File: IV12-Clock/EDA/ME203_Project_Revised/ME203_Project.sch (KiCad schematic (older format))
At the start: 27 parts, among them J1 Conn_01x12, J10 Conn_01x01, J11 Conn_01x02, J12 Conn_01x01, J13 Conn_01x02, J2 Conn_01x05, J6 Conn_01x07

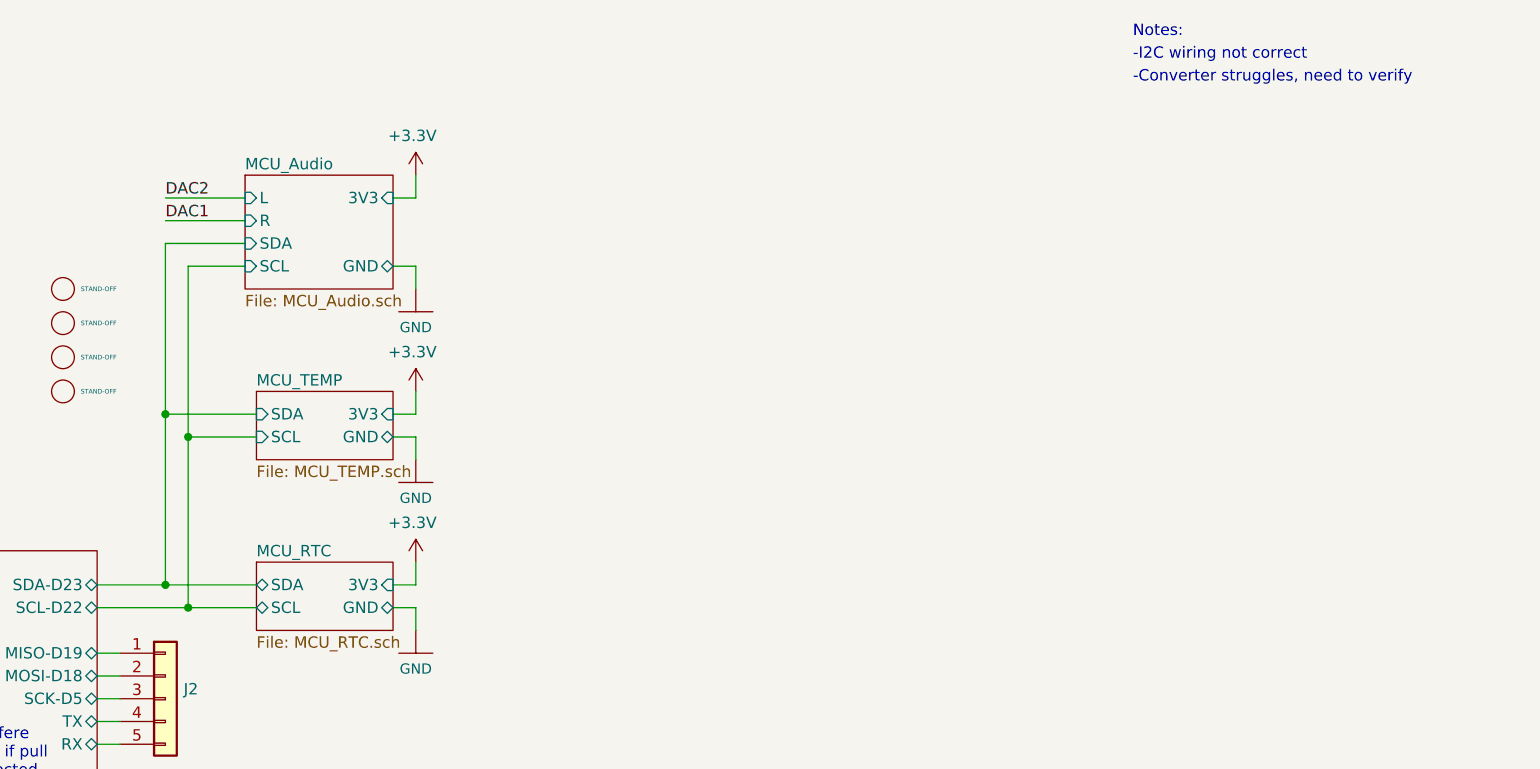
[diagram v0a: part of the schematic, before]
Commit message: Added touch buttons for speakers (untested)
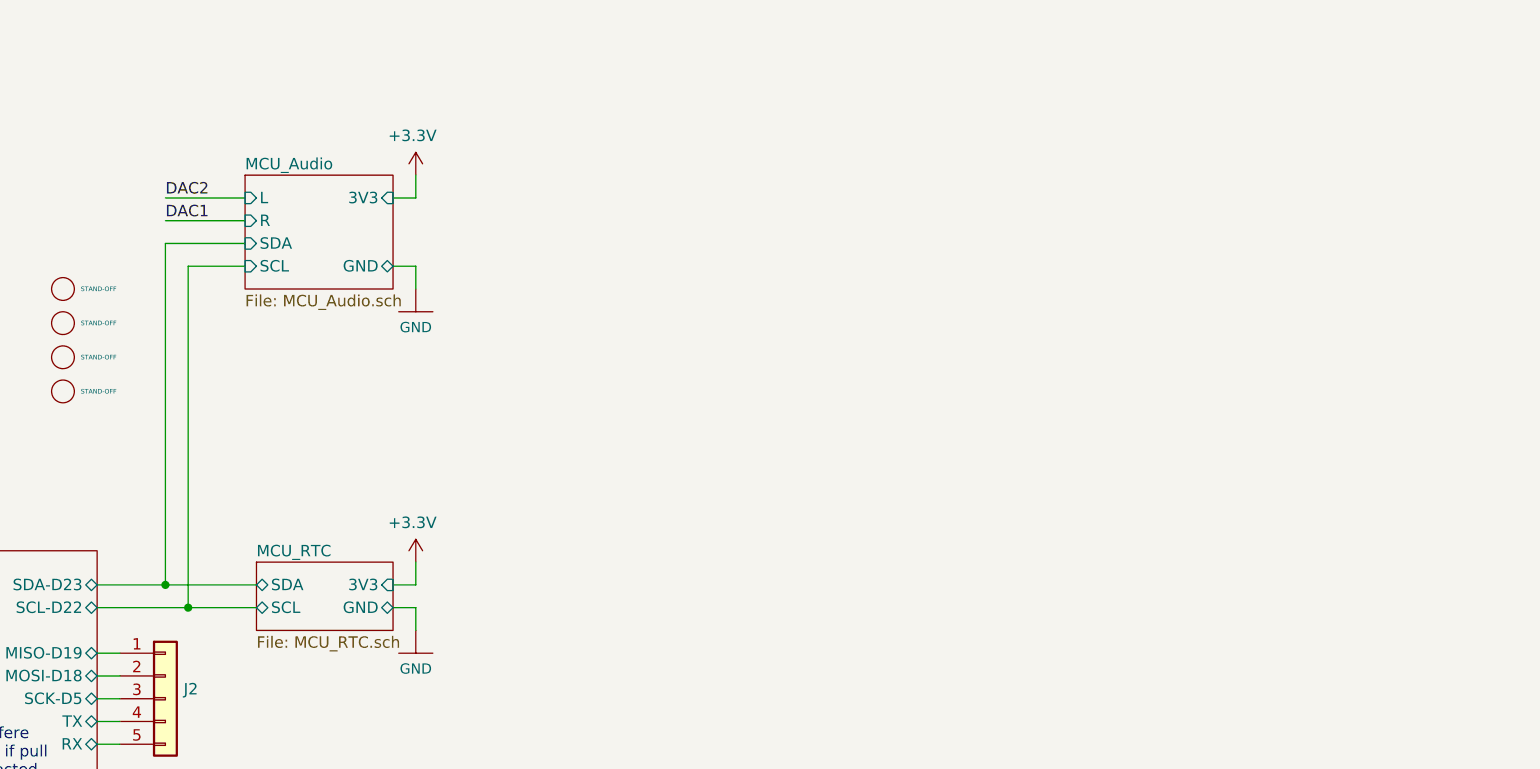
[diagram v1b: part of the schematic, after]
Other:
- note removed: "-Converter struggles, need to verify"
- note removed: "-I2C wiring not correct"
- note removed: "Notes:"
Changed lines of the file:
@@
 $Descr A4 11693 8268
 encoding utf-8
-Sheet 1 8
+Sheet 1 7
 Title ""
 Date ""
@@
 Wire Wire Line
 	2800 4500 2800 4600
-$Sheet
-S 5900 2250 600  300
-U 5CCEB9C5
-F0 "MCU_TEMP" 50
-F1 "MCU_TEMP.sch" 50
-F2 "SCL" I L 5900 2450 50
-F3 "GND" B R 6500 2450 50
-F4 "3V3" I R 6500 2350 50
-F5 "SDA" I L 5900 2350 50
-$EndSheet
 $Comp
 L SparkFun-PowerSymbols:GND #GND0123
@@
 	1    0    0    -1
 $EndComp
-Wire Wire Line
-	6600 2250 6600 2350
-Wire Wire Line
-	6600 2450 6600 2550
-$Comp
-L power:+3.3V #PWR0122
-U 1 1 5CCF9E67
-P 6600 2250
-F 0 "#PWR0122" H 6600 2100 50  0001 C CNN
-F 1 "+3.3V" H 6615 2423 50  0000 C CNN
-F 2 "" H 6600 2250 50  0001 C CNN
-F 3 "" H 6600 2250 50  0001 C CNN
-	1    6600 2250
-	-1   0    0    -1
-$EndComp
-$Comp
-L SparkFun-PowerSymbols:GND #GND0124
-U 1 1 5CCF9E6D
-P 6600 2550
-F 0 "#GND0124" H 6650 2500 45  0001 L BNN
-F 1 "GND" H 6600 2381 45  0000 C CNN
-F 2 "" H 6600 2450 60  0001 C CNN
-F 3 "" H 6600 2450 60  0001 C CNN
-	1    6600 2550
-	1    0    0    -1
-$EndComp
-Wire Wire Line
-	6500 2450 6600 2450
-Wire Wire Line
-	6600 2350 6500 2350
-Wire Wire Line
-	5500 3100 5500 2350
-Wire Wire Line
-	5500 2350 5900 2350
 Connection ~ 5500 3100
 Wire Wire Line
 	5500 3100 5900 3100
-Wire Wire Line
-	5900 2450 5600 2450
-Wire Wire Line
-	5600 2450 5600 3200
 Connection ~ 5600 3200
 Wire Wire Line
@@
 F7 "3V3" I R 6500 1400 50
 $EndSheet
-Connection ~ 5600 2450
-Connection ~ 5500 2350
-Wire Wire Line
-	5600 1700 5600 2450
-Wire Wire Line
-	5500 1600 5500 2350
 Wire Wire Line
 	5600 1700 5850 1700
@@
 	1    0    0    -1
 $EndComp
-Text Notes 9750 700  0    50   ~ 0
-Notes:
-Text Notes 9750 800  0    50   ~ 0
--I2C wiring not correct
-Text Notes 9750 900  0    50   ~ 0
--Converter struggles, need to verify
+Wire Wire Line
+	5500 1600 5500 3100
+Wire Wire Line
+	5600 1700 5600 3200
 $EndSCHEMATC
